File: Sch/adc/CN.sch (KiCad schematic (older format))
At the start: 25 parts, among them J1 JP2, J2 JP2, P1 CONN_02X40, U1 LTC2292

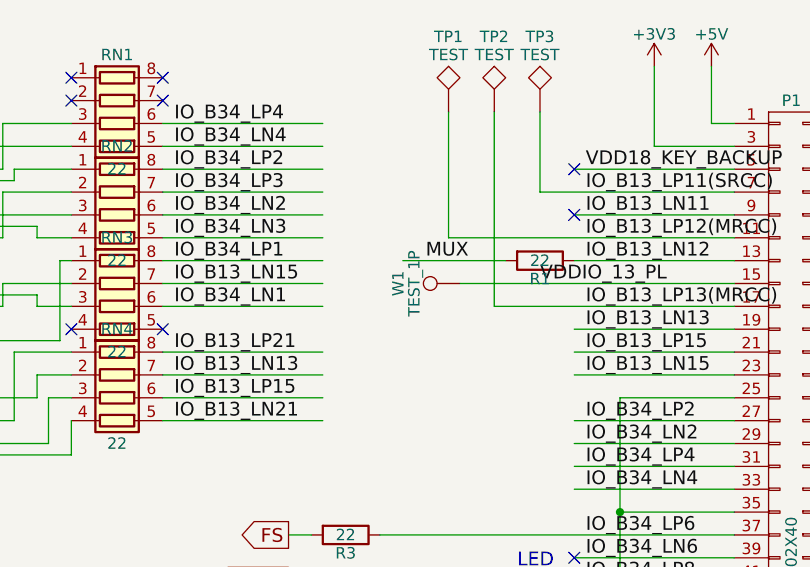
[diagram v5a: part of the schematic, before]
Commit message: Start redesign of ADC board
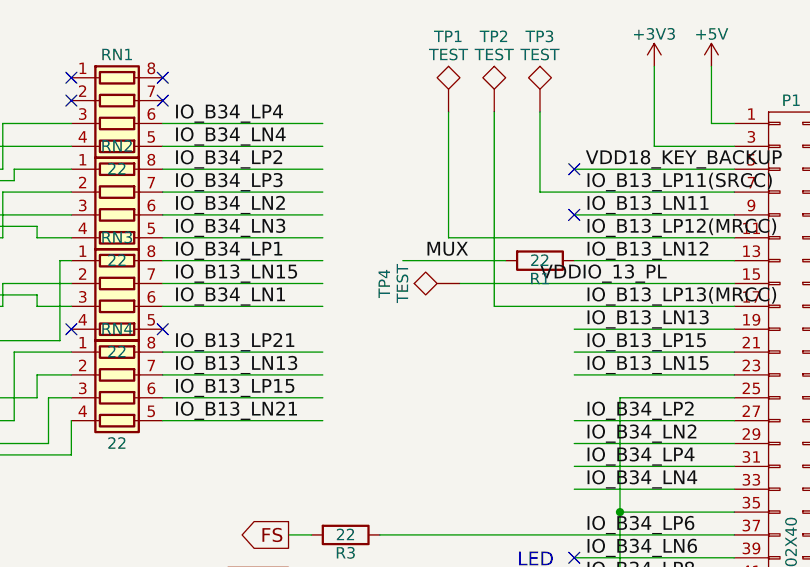
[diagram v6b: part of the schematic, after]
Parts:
- removed W1: TEST_1P, adc_lib:68000-401HLF, symbol TEST_1P
- added TP4: TEST, adc_lib:TL, symbol TEST
- J1, J2: footprint (none) -> adc_lib:M20-9980245
- R3, R4, R9: footprint (none) -> adc_lib:R0603
- TP1, TP2, TP3: footprint (none) -> adc_lib:TL
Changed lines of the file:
@@
-$EndComp
-$Comp
-L TEST_1P W1
-U 1 1 58A9D9D4
-P 5450 2450
-F 0 "W1" H 5450 2720 50  0000 C CNN
-F 1 "TEST_1P" H 5450 2650 50  0000 C CNN
-F 2 "adc_lib:68000-401HLF" H 5650 2450 50  0001 C CNN
-F 3 "" H 5650 2450 50  0000 C CNN
-	1    5450 2450
-	0    -1   -1   0
 $EndComp
 $Comp
@@
 F 0 "J1" H 2600 5700 60  0000 C CNN
 F 1 "JP2" H 2600 6150 60  0000 C CNN
-F 2 "" H 2550 6050 60  0001 C CNN
+F 2 "adc_lib:M20-9980245" H 2550 6050 60  0001 C CNN
 F 3 "" H 2550 6050 60  0001 C CNN
 	1    2600 5950
@@
 F 0 "R4" V 5030 3750 50  0000 C CNN
 F 1 "22" V 4950 3750 50  0000 C CNN
-F 2 "" V 4880 3750 50  0000 C CNN
+F 2 "adc_lib:R0603" V 4880 3750 50  0001 C CNN
 F 3 "" H 4950 3750 50  0000 C CNN
 	1    4950 3750
@@
 F 0 "R3" V 5030 3550 50  0000 C CNN
 F 1 "22" V 4950 3550 50  0000 C CNN
-F 2 "" V 4880 3550 50  0000 C CNN
+F 2 "adc_lib:R0603" V 4880 3550 50  0001 C CNN
 F 3 "" H 4950 3550 50  0000 C CNN
 	1    4950 3550
@@
 F 0 "R9" V 5030 3850 50  0000 C CNN
 F 1 "22" V 4950 3850 50  0000 C CNN
-F 2 "" V 4880 3850 50  0000 C CNN
+F 2 "adc_lib:R0603" V 4880 3850 50  0001 C CNN
 F 3 "" H 4950 3850 50  0000 C CNN
 	1    4950 3850
@@
 F 0 "J2" H 10100 3400 60  0000 C CNN
 F 1 "JP2" H 10100 3850 60  0000 C CNN
-F 2 "" H 10050 3750 60  0001 C CNN
+F 2 "adc_lib:M20-9980245" H 10050 3750 60  0001 C CNN
 F 3 "" H 10050 3750 60  0001 C CNN
 	1    10100 3650
@@
 F 0 "TP3" H 5800 2000 50  0000 C BNN
 F 1 "TEST" H 5800 1950 50  0000 C CNN
-F 2 "" H 5800 1700 50  0000 C CNN
+F 2 "adc_lib:TL" H 5800 1700 50  0001 C CNN
 F 3 "" H 5800 1700 50  0000 C CNN
 	1    5800 1700
@@
 F 0 "TP2" H 5600 2000 50  0000 C BNN
 F 1 "TEST" H 5600 1950 50  0000 C CNN
-F 2 "" H 5600 1700 50  0000 C CNN
+F 2 "adc_lib:TL" H 5600 1700 50  0001 C CNN
 F 3 "" H 5600 1700 50  0000 C CNN
 	1    5600 1700
@@
 F 0 "TP1" H 5400 2000 50  0000 C BNN
 F 1 "TEST" H 5400 1950 50  0000 C CNN
-F 2 "" H 5400 1700 50  0000 C CNN
+F 2 "adc_lib:TL" H 5400 1700 50  0001 C CNN
 F 3 "" H 5400 1700 50  0000 C CNN
 	1    5400 1700
@@
 NoConn ~ 8150 2250
 NoConn ~ 8150 2350
+$Comp
+L TEST TP4
+U 1 1 5980E1B4
+P 5450 2450
+F 0 "TP4" H 5450 2750 50  0000 C BNN
+F 1 "TEST" H 5450 2700 50  0000 C CNN
+F 2 "adc_lib:TL" H 5450 2450 50  0001 C CNN
+F 3 "" H 5450 2450 50  0000 C CNN
+	1    5450 2450
+	0    -1   -1   0
+$EndComp
 $EndSCHEMATC

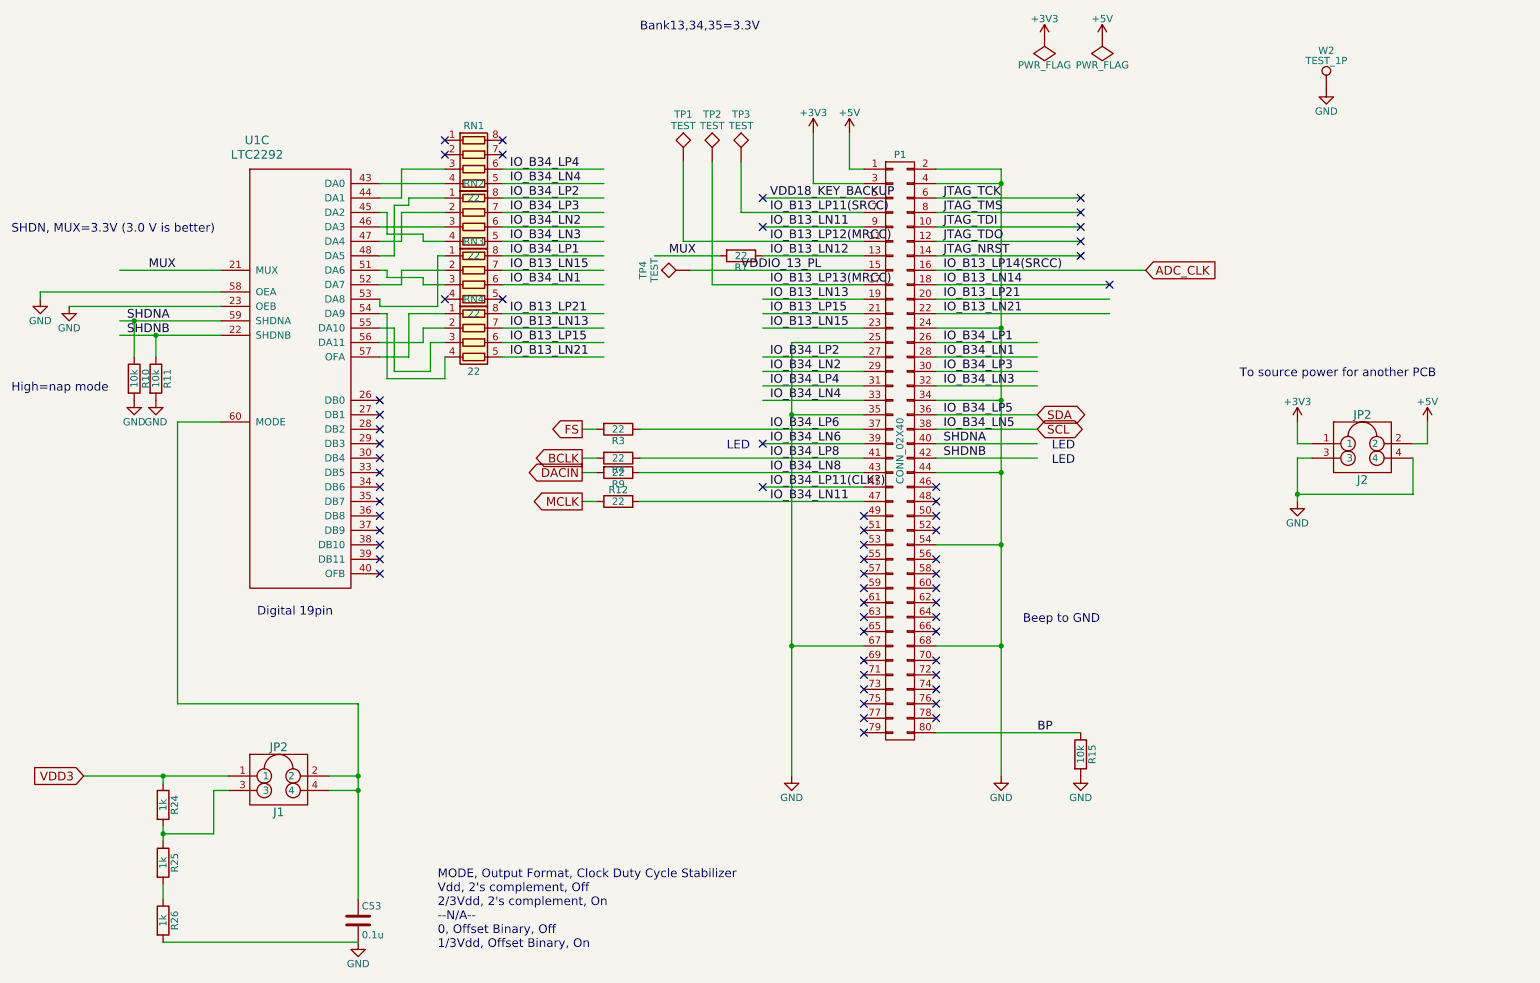
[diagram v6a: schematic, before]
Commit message: ADC PCB layout in progress
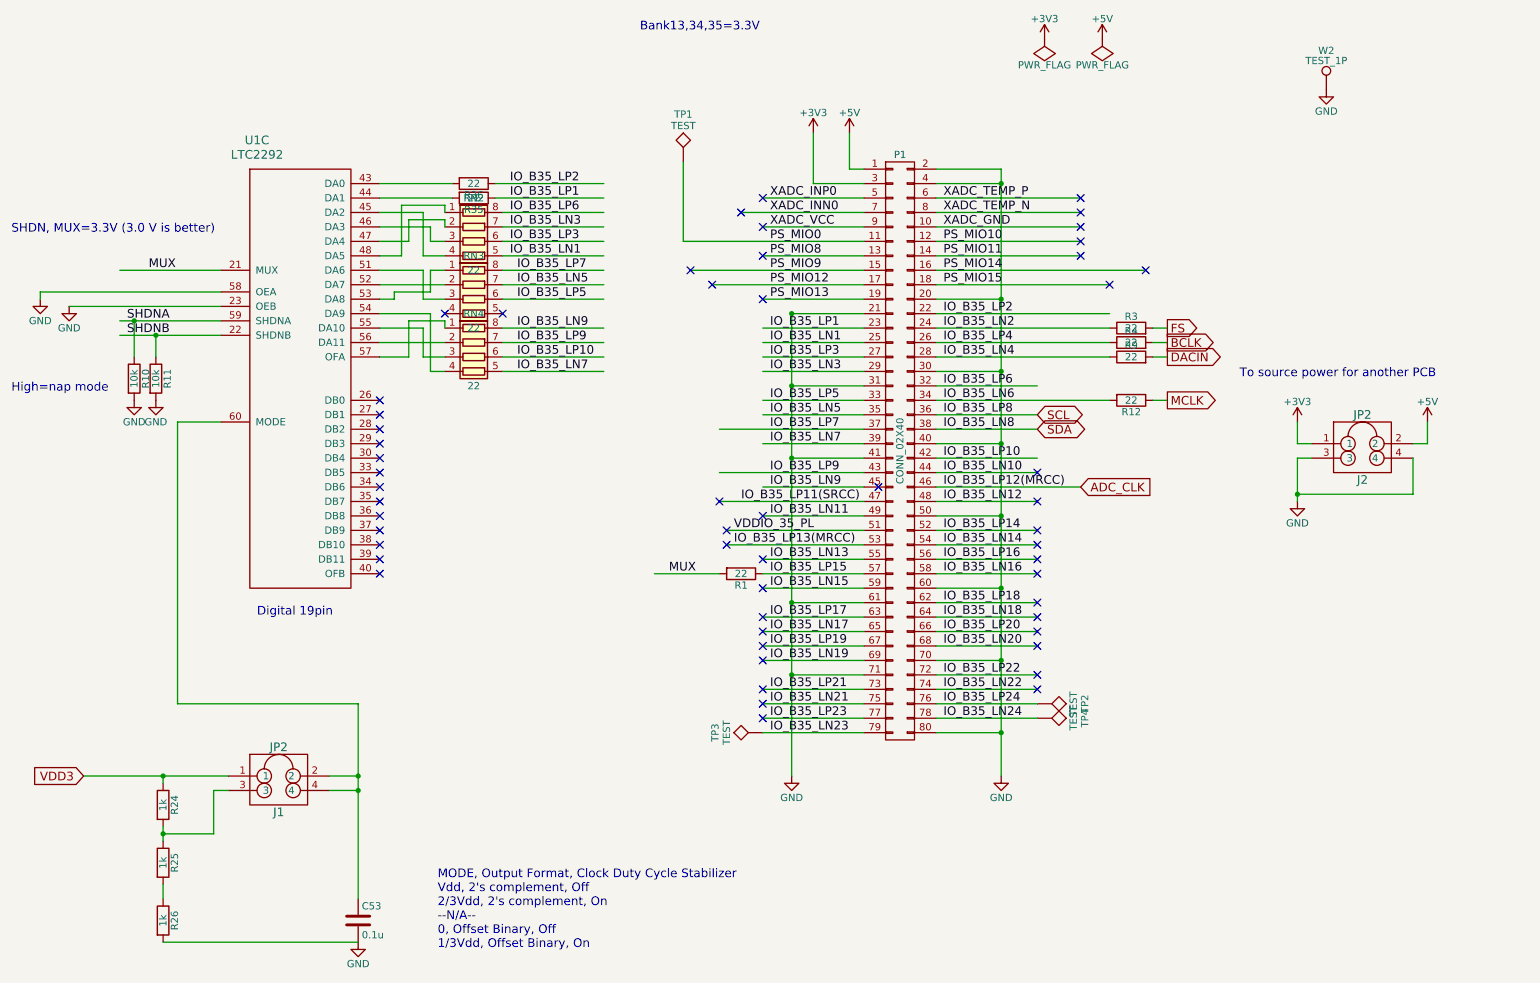
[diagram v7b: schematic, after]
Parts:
- removed R15: 10k, adc_lib:R0603, symbol R
- removed RN1: 22, adc_lib:EXB-38V220JV, symbol R_Pack04
- added R35, R36: 22, adc_lib:R0402, symbol R
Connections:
- net labels added: IO_B35_LN1, IO_B35_LN10, IO_B35_LN11, IO_B35_LN12, IO_B35_LN13, IO_B35_LN14, IO_B35_LN15, IO_B35_LN16, IO_B35_LN17, IO_B35_LN18, IO_B35_LN19, IO_B35_LN2, IO_B35_LN20, IO_B35_LN21, IO_B35_LN22, IO_B35_LN23, IO_B35_LN24, IO_B35_LN3, IO_B35_LN4, IO_B35_LN5, IO_B35_LN6, IO_B35_LN7, IO_B35_LN8, IO_B35_LN9, IO_B35_LP1, IO_B35_LP10, IO_B35_LP11(SRCC), IO_B35_LP12(MRCC), IO_B35_LP13(MRCC), IO_B35_LP14, IO_B35_LP15, IO_B35_LP16, IO_B35_LP17, IO_B35_LP18, IO_B35_LP19, IO_B35_LP2, IO_B35_LP20, IO_B35_LP21, IO_B35_LP22, IO_B35_LP23, IO_B35_LP24, IO_B35_LP3, IO_B35_LP4, IO_B35_LP5, IO_B35_LP6, IO_B35_LP7, IO_B35_LP8, IO_B35_LP9, PS_MIO0, PS_MIO10, PS_MIO11, PS_MIO12, PS_MIO13, PS_MIO14, PS_MIO15, PS_MIO8, PS_MIO9, VDDIO_35_PL, XADC_GND, XADC_INN0, XADC_INP0, XADC_TEMP_N, XADC_TEMP_P, XADC_VCC
- net labels removed: BP, IO_B13_LN11, IO_B13_LN12, IO_B13_LN13, IO_B13_LN14, IO_B13_LN15, IO_B13_LN21, IO_B13_LP11(SRCC), IO_B13_LP12(MRCC), IO_B13_LP13(MRCC), IO_B13_LP14(SRCC), IO_B13_LP15, IO_B13_LP21, IO_B34_LN1, IO_B34_LN11, IO_B34_LN2, IO_B34_LN3, IO_B34_LN4, IO_B34_LN5, IO_B34_LN6, IO_B34_LN8, IO_B34_LP1, IO_B34_LP11(CLK?), IO_B34_LP2, IO_B34_LP3, IO_B34_LP4, IO_B34_LP5, IO_B34_LP6, IO_B34_LP8, JTAG_NRST, JTAG_TCK, JTAG_TDI, JTAG_TDO, JTAG_TMS, VDD18_KEY_BACKUP, VDDIO_13_PL
- wire segments 150 -> 169
- no-connect marks 59 -> 55
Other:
- note removed: "Beep to GND"
- note removed: "LED"
- moved on the sheet: R1, R12, R3, R4, R9, RN2, RN3, RN4, TP2, TP3, TP4
